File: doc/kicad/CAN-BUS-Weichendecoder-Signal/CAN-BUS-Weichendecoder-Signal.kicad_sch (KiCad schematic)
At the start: 41 parts, among them J1 Conn_01x04_Male, J11 250-1406, J12 Wago 250-1406, J13 Wago 250-1406, J14 Wago 250-1406, J15 Wago 250-1406, J16 Wago 250-1406, J21 Conn_01x06, J22 Conn_01x06, J23 Conn_01x06, J24 Conn_01x06, J25 Conn_01x06, J26 Conn_01x06, J31 RJ12, J32 RJ12, J33 RJ12, J34 RJ12, J35 RJ12, J36 RJ12, J5 Conn_01x03, U1 PCF8574, U2 PCF8574, U3 PCF8574, U4 PCF8574, U5 ULN2803A, U6 ULN2803A, U7 ULN2803A, U8 ULN2803A

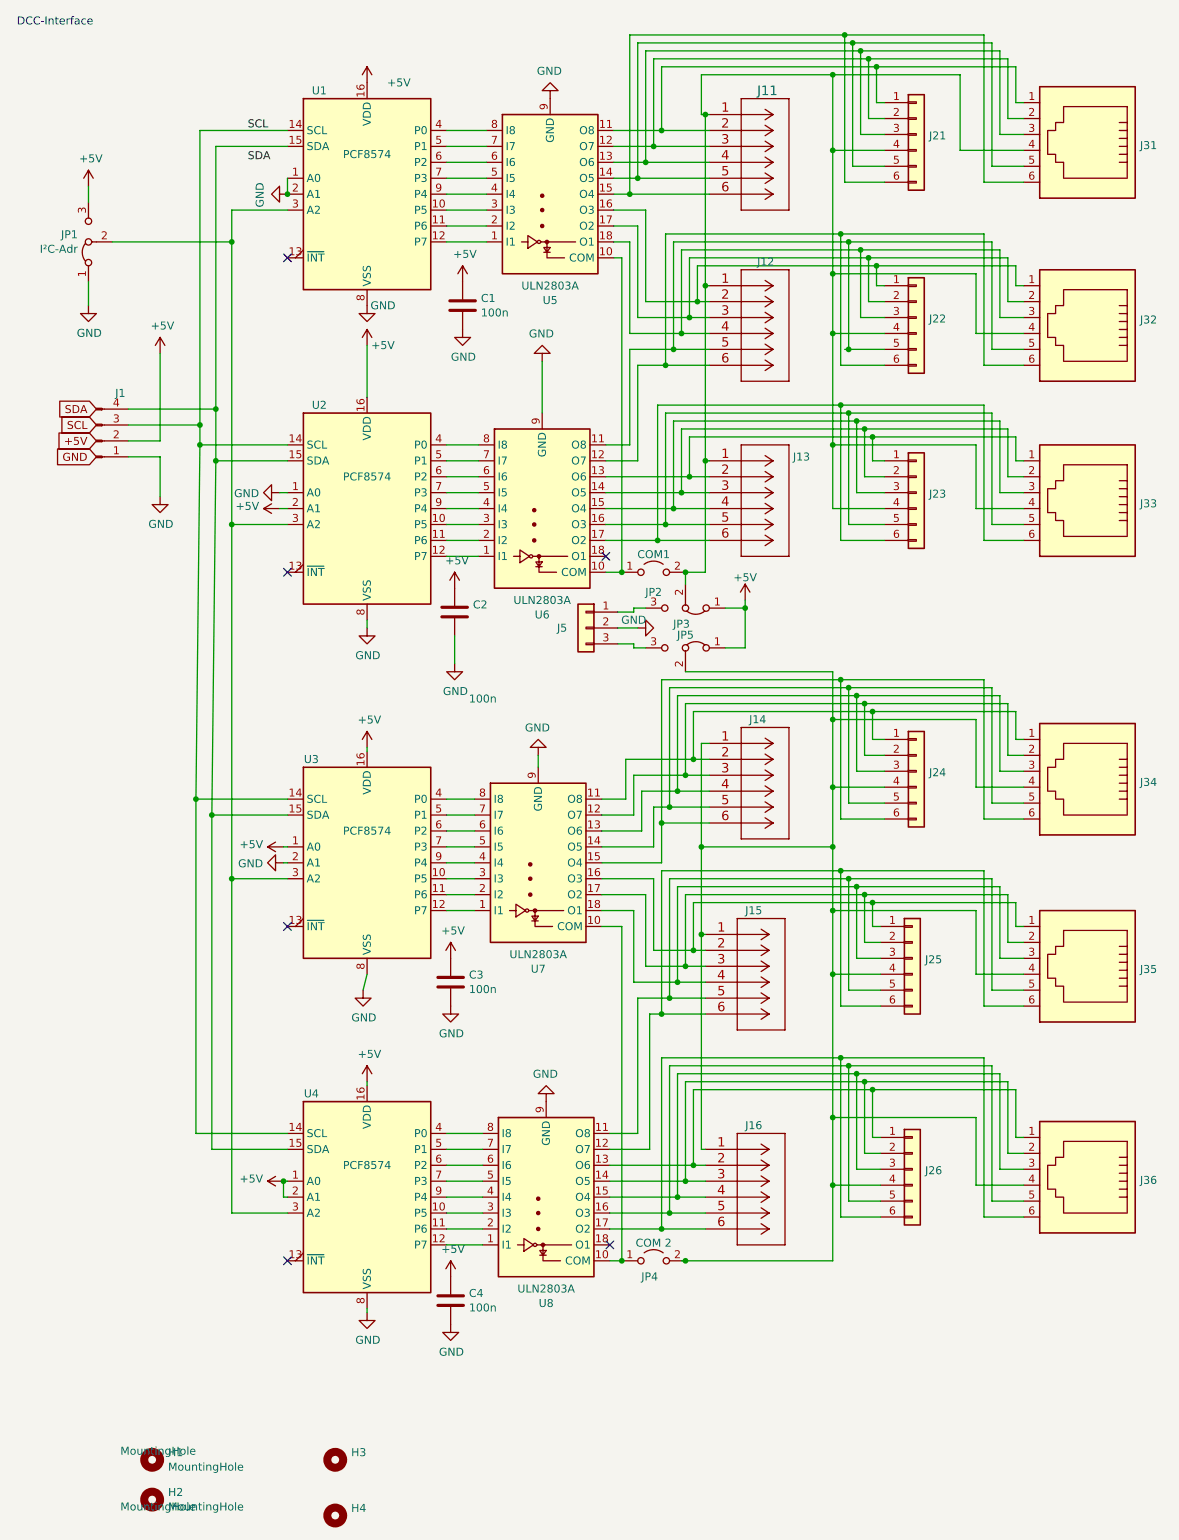
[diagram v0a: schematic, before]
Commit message: Pullup-Widerstand hinzugefügt; Power-LED hinzugefügt
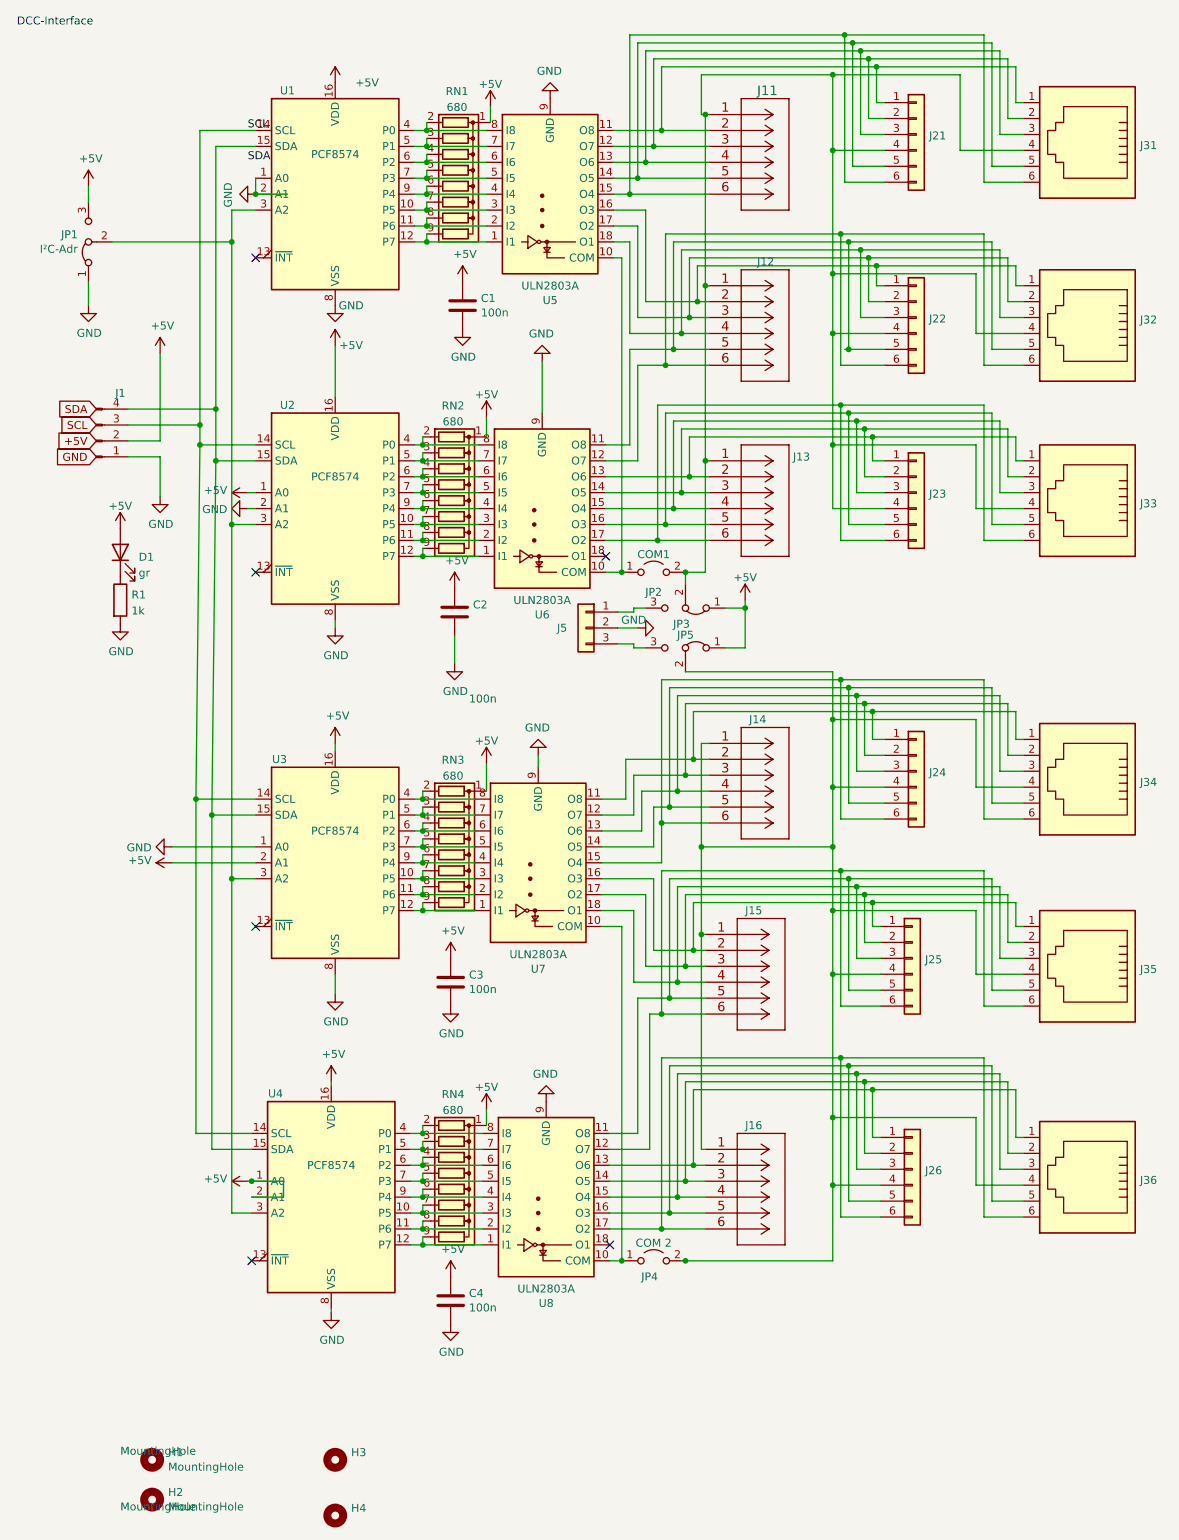
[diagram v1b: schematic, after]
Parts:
- added D1: gr, LED_THT:LED_D3.0mm, symbol Device:LED
- added R1: 1k, Resistor_THT:R_Axial_DIN0207_L6.3mm_D2.5mm_P7.62mm_Horizontal, symbol Device:R
- added RN1, RN2, RN3, RN4: 680, Resistor_THT:R_Array_SIP9, symbol Device:R_Network08
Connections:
- net +5V: now also U2.1 (A0), U3.2 (A1), D1.2 (A), RN1.1 (common), RN2.1 (common), RN3.1 (common), RN4.1 (common); no longer U2.2 (A1), U3.1 (A0)
- net GND: now also U2.2 (A1), U3.1 (A0), R1.2; no longer U2.1 (A0), U3.2 (A1)
- net at U1.10 (P5), U5.3 (I3): now also RN1.7 (R6)
- net at U1.11 (P6), U5.2 (I2): now also RN1.8 (R7)
- net at U1.12 (P7), U5.1 (I1): now also RN1.9 (R8)
- net at U1.4 (P0), U5.8 (I8): now also RN1.2 (R1)
- net at U1.5 (P1), U5.7 (I7): now also RN1.3 (R2)
- net at U1.6 (P2), U5.6 (I6): now also RN1.4 (R3)
- net at U1.7 (P3), U5.5 (I5): now also RN1.5 (R4)
- net at U1.9 (P4), U5.4 (I4): now also RN1.6 (R5)
- net at U2.10 (P5), U6.3 (I3): now also RN2.7 (R6)
- net at U2.11 (P6), U6.2 (I2): now also RN2.8 (R7)
- net at U2.12 (P7), U6.1 (I1): now also RN2.9 (R8)
- net at U2.4 (P0), U6.8 (I8): now also RN2.2 (R1)
- net at U2.5 (P1), U6.7 (I7): now also RN2.3 (R2)
- net at U2.6 (P2), U6.6 (I6): now also RN2.4 (R3)
- net at U2.7 (P3), U6.5 (I5): now also RN2.5 (R4)
- net at U2.9 (P4), U6.4 (I4): now also RN2.6 (R5)
- net at U3.12 (P7), U7.1 (I1): now also RN3.9 (R8)
- net at U3.11 (P6), U7.2 (I2): now also RN3.8 (R7)
- net at U3.10 (P5), U7.3 (I3): now also RN3.7 (R6)
- net at U3.9 (P4), U7.4 (I4): now also RN3.6 (R5)
- net at U3.7 (P3), U7.5 (I5): now also RN3.5 (R4)
- net at U3.6 (P2), U7.6 (I6): now also RN3.4 (R3)
- net at U3.5 (P1), U7.7 (I7): now also RN3.3 (R2)
- net at U3.4 (P0), U7.8 (I8): now also RN3.2 (R1)
- net at U4.12 (P7), U8.1 (I1): now also RN4.9 (R8)
- net at U4.11 (P6), U8.2 (I2): now also RN4.8 (R7)
- net at U4.10 (P5), U8.3 (I3): now also RN4.7 (R6)
- net at U4.9 (P4), U8.4 (I4): now also RN4.6 (R5)
- net at U4.7 (P3), U8.5 (I5): now also RN4.5 (R4)
- net at U4.6 (P2), U8.6 (I6): now also RN4.4 (R3)
- net at U4.5 (P1), U8.7 (I7): now also RN4.3 (R2)
- net at U4.4 (P0), U8.8 (I8): now also RN4.2 (R1)
- new net: D1.1 (K), R1.1
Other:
- moved on the sheet: U1, U2, U3, U4
